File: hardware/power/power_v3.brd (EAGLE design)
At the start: 92 x 92 mm, 32 parts, among them J1 LINEAR_2_5040500291, J2 PWR_2_XT30PW-F, J3 PWR_2_XT30PW-F, J4 PWR_2_XT30PW-F, J5 PWR_2_XT30PW-F, Q1 CSD19536KTT, U1 PDQ30-Q24-S5-D, U2 PDQ30-Q24-S12-D, U3 LM5069

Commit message: Spinning IC
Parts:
- added C12: 0.068uF 50V, _T_rcl:C0603
- added C13: 0.012uF 50V, _T_rcl:C0603
- added D3: SCHOTTKY_SOD123, _T_rcl:SOD123
- added D4: D, _T_rcl:SOD123
- added J10: LINEAR_2_5040500291, _T_conn:MOLEX_5040500291
- added J6, J7: FASTON, _T_power:FASTON_1289-ST
- added J8, J9: PWR_4, _T_conn:MOLEX_4_RA
- added Q2: CSD19536KTT, _T_transistors:TO-263
- added R10: 20k, _T_rcl:R0603
- added R11: 2.4, _T_rcl:R0603
- added R12: 10, _T_rcl:R0603
- added R13: 47k 1%, _T_rcl:R0603
- added R14: 2.7k 1%, _T_rcl:R0603
- added R15: 4.7k 1%, _T_rcl:R0603
- added R16: 1k, _T_rcl:R0603
- added R9: .002, _T_rcl:R2512_KELVIN
- added U4: LM5069, _T_ic:VSSOP_10
- moved C1 92.4 mm to (103.3, 52.3)
- moved C2 92.4 mm to (108.9, 67.8)
- moved D2 92.4 mm to (126.2, 59.9)
- moved R1 92.4 mm to (102.3, 62.1)
- moved R2 92.4 mm to (107.1, 58.6)
- moved R4 92.4 mm to (102.0, 58.6)
- moved R5 92.4 mm to (110.9, 58.6)
- moved R6 92.4 mm to (121.1, 58.6)
- moved R7 92.4 mm to (116.0, 58.6)
- moved U3 92.4 mm to (101.9, 72.3)
- moved D1 92.4 mm to (115.3, 67.3)
- moved R3 92.4 mm to (104.6, 58.6)
- moved R8 92.4 mm to (99.5, 58.6)
- moved L2 37.6 mm to (18.0, 69.0), turned to 90 degrees
- moved C11 34.6 mm to (8.50, 68.5), turned to 180 degrees
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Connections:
- new net N$14: Q2.2, R9.2A, R9.2B
- new net N$15: C12.1, U4.6
- new net N$16: R10.2, U4.7
- new net N$17: R11.1, R12.1, U4.1
- new net N$18: R11.2, R9.2_KELVIN
- new net N$19: R13.1, R14.2, U4.3
- new net N$20: R14.1, R15.2, U4.4
- new net N$21: J10.P1, R13.2
- new net N$22: R12.2, R9.1_KELVIN
- new net N$23: C13.1, D4.C
- new net N$24: D4.A, Q2.1, R16.2, U4.10
- net +12V: now also J9.CIRCUIT2, J9.CIRCUIT4
- net +24V_ISO: now also D3.C, Q2.3, U4.9
- net +5V: now also J8.CIRCUIT2, J8.CIRCUIT4
- net +V_BATT: now also J10.P2, J6.P$1, J6.P$2, R9.1A, R9.1B, U4.2
- net -V_BATT: now also C12.2, C13.2, D3.A, J7.P$1, J7.P$2, R10.1, R15.1, R16.1, U4.5
- net 12V_GND: now also J9.CIRCUIT1, J9.CIRCUIT3
- net 5V_GND: now also J8.CIRCUIT1, J8.CIRCUIT3
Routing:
- net -V_BATT: track 0.00 -> 110.8 mm, vias 0 -> 15
- net N$24: track 0.00 -> 55.9 mm, vias 0 -> 2
- net +12V: track 0.00 -> 43.4 mm
- net +V_BATT: track 0.00 -> 40.9 mm, vias 0 -> 1
- net 12V_GND: track 0.00 -> 39.2 mm
- net N$13: track 0.00 -> 38.7 mm
- net +24V_ISO: track 0.00 -> 36.7 mm
- net N$21: track 0.00 -> 34.5 mm
- net N$22: track 0.00 -> 29.3 mm
- net N$18: track 0.00 -> 26.6 mm
- net 5V_GND: track 0.00 -> 17.7 mm
- net N$17: track 0.00 -> 17.3 mm, vias 0 -> 2
- net N$15: track 0.00 -> 13.1 mm, vias 0 -> 2
- net N$16: track 0.00 -> 11.4 mm, vias 0 -> 2
- net N$19: track 0.00 -> 11.3 mm
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- added copper zone on layer 1, net +24V_ISO
- added copper zone on layer 1, net +24V_POWER
- added copper zone on layer 1, net +V_BATT
- added copper zone on layer 2, net +V_BATT
- added copper zone on layer 1, net N$14

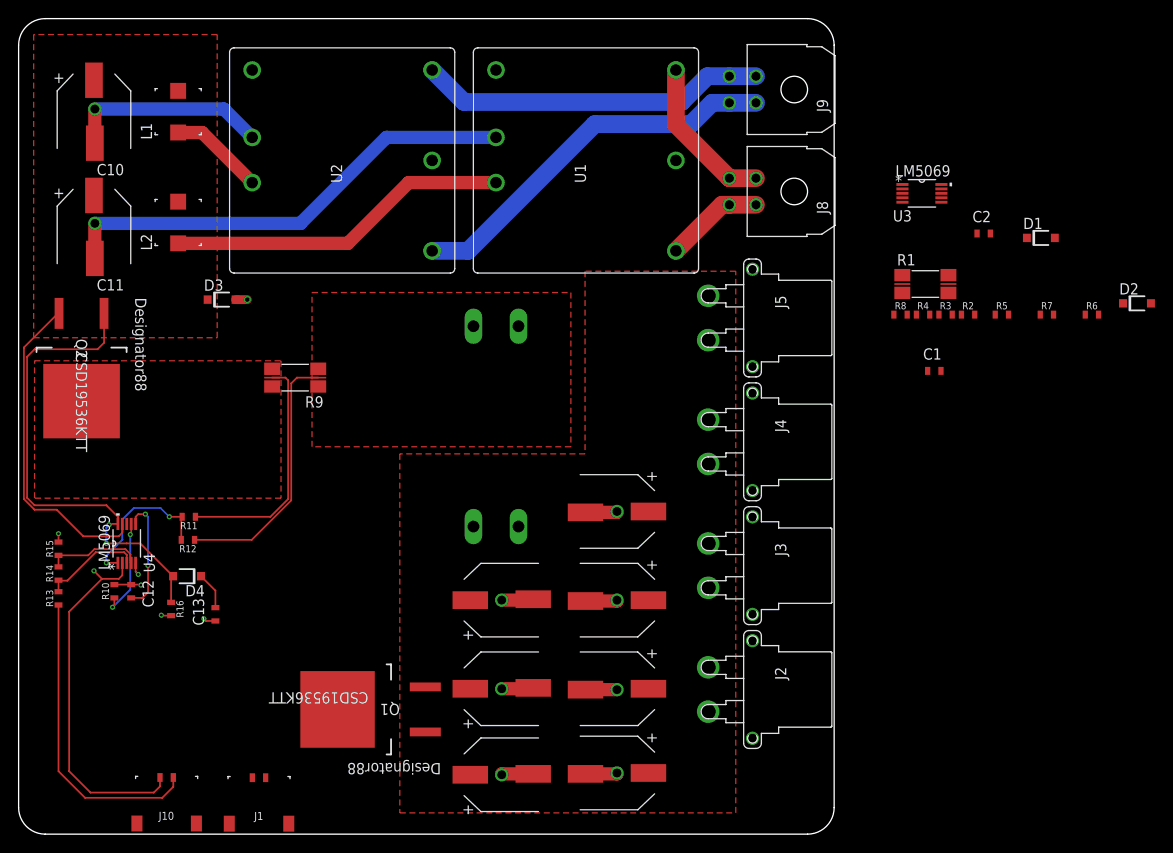
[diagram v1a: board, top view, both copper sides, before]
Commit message: Still need flyback diode
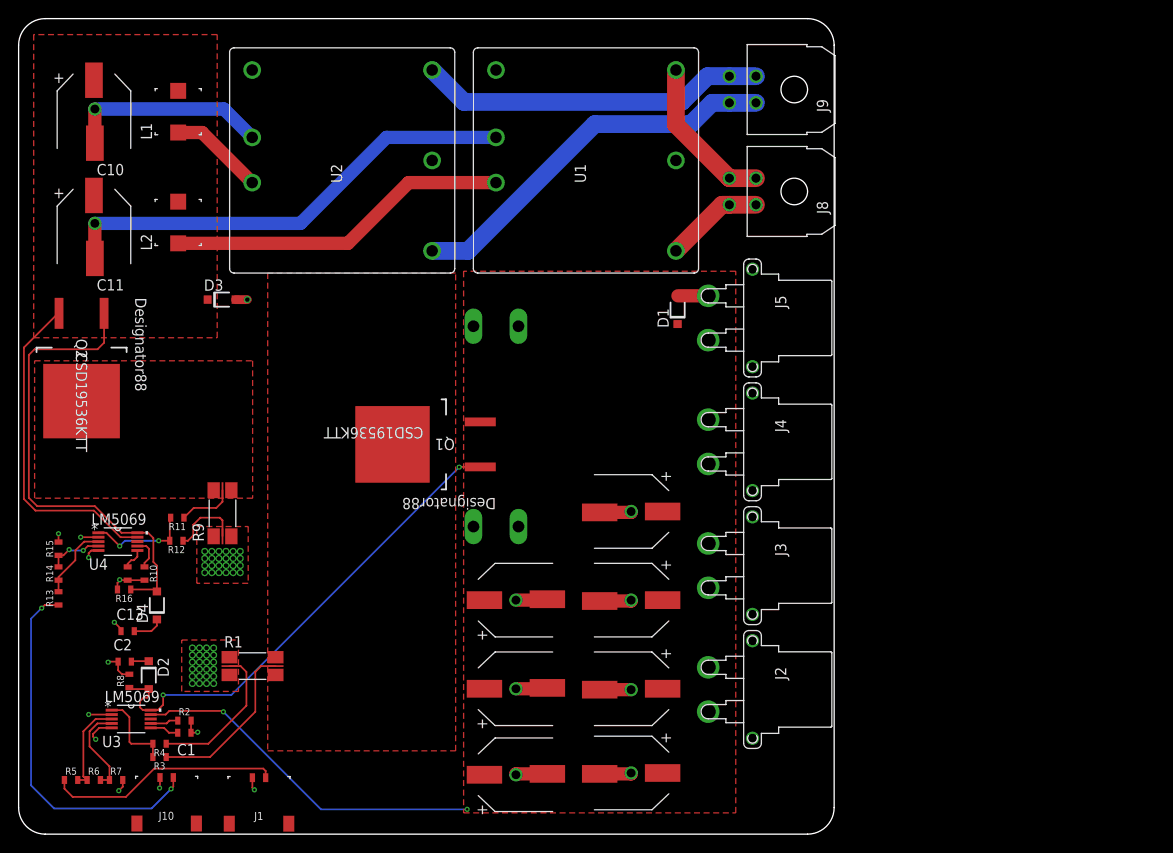
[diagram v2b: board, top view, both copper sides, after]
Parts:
- moved R6 124.2 mm to (8.48, 6.11)
- moved D2 119.1 mm to (14.7, 17.9), turned to 270 degrees
- moved R5 117.4 mm to (5.92, 6.11)
- moved R7 117.4 mm to (11.0, 6.11)
- moved C2 108.3 mm to (12.0, 19.5)
- moved U3 107.1 mm to (12.7, 13.0)
- moved R3 101.8 mm to (15.9, 8.70), turned to 180 degrees
- moved R2 99.6 mm to (18.7, 12.8)
- moved R4 98.8 mm to (15.9, 10.2), turned to 180 degrees
- moved R8 96.3 mm to (12.5, 17.3), turned to 90 degrees
- moved C1 93.9 mm to (18.7, 11.4), turned to 180 degrees
- moved R1 87.3 mm to (26.4, 19.0)
- moved D1 41.8 mm to (74.3, 59.1), turned to 90 degrees
- moved Q1 30.5 mm to (45.9, 44.0)
- moved R9 17.4 mm to (23.0, 36.2), turned to 90 degrees
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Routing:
- net N$2: track 0.00 -> 55.5 mm, vias 0 -> 2
- net +24V_POWER: track 0.00 -> 40.5 mm, vias 0 -> 2
- net +V_BATT: track 40.9 -> 7.29 mm, vias 1 -> 52
- net N$7: track 0.00 -> 26.3 mm
- net N$22: track 29.3 -> 8.15 mm
- net N$18: track 26.6 -> 6.40 mm
- net N$6: track 0.00 -> 19.2 mm
- net N$10: track 0.00 -> 16.8 mm
- net -V_BATT: track 110.8 -> 124.5 mm, vias 15 -> 18
- net N$15: track 13.1 -> 2.48 mm, vias 2 -> 0
- net N$8: track 0.00 -> 10.5 mm
- net N$9: track 0.00 -> 10.3 mm
- net N$5: track 0.00 -> 9.36 mm
- net N$16: track 11.4 -> 3.68 mm, vias 2 -> 0
- net N$21: track 34.5 -> 41.7 mm, vias 0 -> 2
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- added copper zone on layer 1, net N$1

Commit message: TVS diodes
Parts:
- added C14: 0.068uF 50V, _T_rcl:C0603
- added D5: 5_0SMDJ24A, _T_rcl:SOD123
- D1, D3: value SCHOTTKY_SOD123 -> 5_0SMDJ24A
- D2: value D -> (none)
- D4: value D -> 1N4148W-7-F
- moved Q2 5.30 mm to (12.4, 52.7)
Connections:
- net +V_BATT: now also C14.1, D5.C
- net -V_BATT: now also C14.2, D5.A
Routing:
- net N$24: track 53.6 -> 59.0 mm
- net +24V_ISO: track 37.2 -> 42.6 mm
- net +V_BATT: track 7.29 -> 10.6 mm, vias 52 -> 53
- net -V_BATT: track 124.5 -> 127.7 mm, vias 18 -> 19

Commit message: Repositioning rsense
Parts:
- moved R1 6.02 mm to (28.0, 24.8)
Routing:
- net N$10: track 16.8 -> 23.4 mm
- net N$6: track 19.2 -> 25.7 mm

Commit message: Ready to PCB it
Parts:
- D2: value (none) -> 1N4148W-7-F
- moved R3 9.96 mm to (21.1, 17.2)
- moved R4 9.96 mm to (21.1, 18.7)
- moved R1 0.90 mm to (28.0, 23.9)
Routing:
- net N$6: track 25.7 -> 13.5 mm
- net N$10: track 23.4 -> 11.5 mm
- net N$5: track 9.36 -> 12.7 mm, vias 0 -> 2

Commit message: Closer routing iso gate and sense
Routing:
- net N$24: track 59.0 -> 36.8 mm, vias 0 -> 2
- net +24V_ISO: track 42.6 -> 24.6 mm, vias 0 -> 2
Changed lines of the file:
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@@
 </layers>
 <board>
-<fusionsync huburn="a.YnVzaW5lc3M6Z21haWwyMjE5MTc" projecturn="a.YnVzaW5lc3M6Z21haWwyMjE5MTcjMjAxOTA2MjkyMDE0MTU5NzY" f3durn="urn:adsk.wipprod:dm.lineage:NIiH3u5URBCqLPNixwQc4w" pcbguid="" lastpulledtime="2020-07-01T23:36:44Z" lastsyncedchangeguid="" latestrevisionid="139082bc-8da4-45ac-b4e8-9beb6a12b33b" lastsyncedrevisionid="139082bc-8da4-45ac-b4e8-9beb6a12b33b" lastboardhashguid="2a13bf80-225b-326f-a644-5012308f9f45" lastpushedtime="2020-07-03T00:46:42Z" linktopcb3d="true"/>
+<fusionsync huburn="a.YnVzaW5lc3M6Z21haWwyMjE5MTc" projecturn="a.YnVzaW5lc3M6Z21haWwyMjE5MTcjMjAxOTA2MjkyMDE0MTU5NzY" f3durn="urn:adsk.wipprod:dm.lineage:NIiH3u5URBCqLPNixwQc4w" pcbguid="" lastpulledtime="2020-07-01T23:36:44Z" lastsyncedchangeguid="" latestrevisionid="a02dffb8-1203-4a76-a1d6-2f53c010d684" lastsyncedrevisionid="a02dffb8-1203-4a76-a1d6-2f53c010d684" lastboardhashguid="31fae87f-55dd-9496-9b75-db9c020a5965" lastpushedtime="2020-07-03T01:54:28Z" linktopcb3d="true"/>
 <plain>
 <wire x1="3" y1="92" x2="0" y2="89" width="0" layer="20" curve="90" locked="yes"/>
@@
 <vertex x="49.9" y="1.3"/>
 <vertex x="81" y="1.3"/>
-<vertex x="81" y="62.7"/>
-<vertex x="49.9" y="62.7"/>
+<vertex x="81" y="63.2"/>
+<vertex x="49.9" y="63.2"/>
 </polygon>
 </signal>
@@
 <contactref element="Q2" pad="3"/>
 <contactref element="D3" pad="C"/>
-<wire x1="1.9" y1="36.5" x2="0.6" y2="37.8" width="0.2" layer="1"/>
-<wire x1="4.55" y1="58.85" x2="9.86" y2="58.85" width="0.2" layer="1"/>
-<wire x1="0.6" y1="37.8" x2="0.6" y2="54.9" width="0.2" layer="1"/>
-<wire x1="0.6" y1="54.9" x2="4.55" y2="58.85" width="0.2" layer="1"/>
-<wire x1="11.5" y1="33.5" x2="13.3971" y2="33.5" width="0.2" layer="1"/>
-<wire x1="1.9" y1="36.5" x2="8.5" y2="36.5" width="0.2" layer="1"/>
-<wire x1="8.5" y1="36.5" x2="11.5" y2="33.5" width="0.2" layer="1"/>
+<wire x1="13.3971" y1="33.5" x2="12.3" y2="33.5" width="0.2" layer="1"/>
+<wire x1="12.3" y1="33.5" x2="12" y2="33.8" width="0.2" layer="1"/>
+<via x="12" y="33.8" extent="1-16" drill="0.29"/>
+<wire x1="12" y1="33.8" x2="12" y2="56.9" width="0.2" layer="16"/>
+<via x="12" y="56.9" extent="1-16" drill="0.29"/>
 </signal>
 <signal name="12V_GND" class="1">
@@
 <contactref element="Q2" pad="1"/>
 <contactref element="U4" pad="10"/>
-<wire x1="14.94" y1="58.85" x2="14.94" y2="55.44" width="0.2" layer="1"/>
-<wire x1="14.94" y1="55.44" x2="14.2" y2="54.7" width="0.2" layer="1"/>
-<wire x1="1.1524" y1="37.945975" x2="2.0991875" y2="36.9991875" width="0.2" layer="1"/>
-<wire x1="8.6008125" y1="36.9991875" x2="2.0991875" y2="36.9991875" width="0.2" layer="1"/>
-<wire x1="14.2" y1="54.7" x2="1.8" y2="54.7" width="0.2" layer="1"/>
-<wire x1="1.8" y1="54.7" x2="1.1524" y2="54.0524" width="0.2" layer="1"/>
-<wire x1="1.1524" y1="54.0524" x2="1.1524" y2="37.945975" width="0.2" layer="1"/>
 <wire x1="12.65" y1="27.6" x2="15.375" y2="27.6" width="0.2" layer="1"/>
 <wire x1="15.375" y1="27.6" x2="15.6" y2="27.375" width="0.2" layer="1"/>
-<wire x1="13.3971" y1="34" x2="11.6" y2="34" width="0.2" layer="1"/>
-<wire x1="11.6" y1="34" x2="8.6008125" y2="36.9991875" width="0.2" layer="1"/>
 <wire x1="15.6" y1="27.375" x2="15.6" y2="30.3" width="0.2" layer="1"/>
 <wire x1="15.2" y1="30.7" x2="15.2" y2="33.4" width="0.2" layer="1"/>
@@
 <wire x1="14.6" y1="34" x2="13.3971" y2="34" width="0.2" layer="1"/>
 <wire x1="15.6" y1="30.3" x2="15.2" y2="30.7" width="0.2" layer="1"/>
+<wire x1="13.3971" y1="34" x2="13.3971" y2="36.6971" width="0.2" layer="1"/>
+<wire x1="13.3971" y1="36.6971" x2="13.4" y2="36.7" width="0.2" layer="1"/>
+<via x="13.4" y="36.7" extent="1-16" drill="0.29"/>
+<wire x1="13.4" y1="36.7" x2="13.4" y2="53.4" width="0.2" layer="16"/>
+<wire x1="13.4" y1="53.4" x2="14.9" y2="54.9" width="0.2" layer="16"/>
+<via x="14.9" y="54.9" extent="1-16" drill="0.29"/>
+<wire x1="14.9" y1="54.9" x2="14.9" y2="58.81" width="0.2" layer="1"/>
+<wire x1="14.9" y1="58.81" x2="14.94" y2="58.85" width="0.2" layer="1"/>
 </signal>
 </signals>

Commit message: Power junctions
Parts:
- moved J8 0.30 mm to (87.2, 72.5)
- moved J9 0.30 mm to (87.2, 84.0)
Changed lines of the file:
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@@
 <attribute name="NAME" x="57.66" y="37.24" locked="yes" size="1.27" layer="22" rot="MR0"/>
 </element>
-<element name="J8" library="_T_conn" library_urn="urn:adsk.eagle:library:19570503" package="MOLEX_4_RA" package3d_urn="urn:adsk.eagle:package:16152611/5" value="PWR_4" x="87.5" y="72.5" smashed="yes" rot="R90">
-<attribute name="NAME" x="91.31" y="69.96" size="1.27" layer="25" rot="R90"/>
-</element>
-<element name="J9" library="_T_conn" library_urn="urn:adsk.eagle:library:19570503" package="MOLEX_4_RA" package3d_urn="urn:adsk.eagle:package:16152611/5" value="PWR_4" x="87.5" y="84" smashed="yes" rot="R90">
-<attribute name="NAME" x="91.31" y="81.46" size="1.27" layer="25" rot="R90"/>
+<element name="J8" library="_T_conn" library_urn="urn:adsk.eagle:library:19570503" package="MOLEX_4_RA" package3d_urn="urn:adsk.eagle:package:16152611/5" value="PWR_4" x="87.2" y="72.5" smashed="yes" rot="R90">
+<attribute name="NAME" x="91.01" y="69.96" size="1.27" layer="25" rot="R90"/>
+</element>
+<element name="J9" library="_T_conn" library_urn="urn:adsk.eagle:library:19570503" package="MOLEX_4_RA" package3d_urn="urn:adsk.eagle:package:16152611/5" value="PWR_4" x="87.2" y="84" smashed="yes" rot="R90">
+<attribute name="NAME" x="91.01" y="81.46" size="1.27" layer="25" rot="R90"/>
 </element>
 <element name="U4" library="_T_ic" library_urn="urn:adsk.eagle:library:19571245" package="VSSOP_10" package3d_urn="urn:adsk.eagle:package:21297470/2" value="LM5069" x="11.2" y="33" smashed="yes">
@@
 <contactref element="J9" pad="CIRCUIT3"/>
 <wire x1="46.65" y1="86.2" x2="50.25" y2="82.6" width="2" layer="16"/>
-<wire x1="77.7" y1="85.5" x2="80.18" y2="85.5" width="2" layer="16"/>
+<wire x1="77.7" y1="85.5" x2="79.88" y2="85.5" width="2" layer="16"/>
 <wire x1="50.25" y1="82.6" x2="74.8" y2="82.6" width="2" layer="16"/>
 <wire x1="74.8" y1="82.6" x2="77.7" y2="85.5" width="2" layer="16"/>
-<wire x1="83.18" y1="85.5" x2="80.18" y2="85.5" width="2" layer="16"/>
+<wire x1="82.88" y1="85.5" x2="79.88" y2="85.5" width="2" layer="16"/>
 </signal>
 <signal name="5V_GND" class="1">
@@
 <contactref element="J8" pad="CIRCUIT3"/>
 <contactref element="J8" pad="CIRCUIT1"/>
-<wire x1="83.18" y1="74" x2="80.18" y2="74" width="2" layer="1"/>
-<wire x1="80.18" y1="74" x2="74.15" y2="80.03" width="2" layer="1"/>
-<wire x1="74.15" y1="80.03" x2="74.15" y2="86.2" width="2" layer="1"/>
+<wire x1="82.88" y1="74" x2="79.88" y2="74" width="2" layer="1"/>
+<wire x1="79.88" y1="74" x2="74.15" y2="79.73" width="2" layer="1"/>
+<wire x1="74.15" y1="79.73" x2="74.15" y2="86.2" width="2" layer="1"/>
 </signal>
 <signal name="+12V" class="1">
@@
 <contactref element="J9" pad="CIRCUIT4"/>
 <contactref element="J9" pad="CIRCUIT2"/>
-<wire x1="83.182" y1="82.5" x2="80.18" y2="82.5" width="2" layer="16"/>
-<wire x1="80.18" y1="82.5" x2="78.2355375" y2="82.5" width="2" layer="16"/>
+<wire x1="82.882" y1="82.5" x2="79.88" y2="82.5" width="2" layer="16"/>
+<wire x1="79.88" y1="82.5" x2="78.2355375" y2="82.5" width="2" layer="16"/>
 <wire x1="78.2355375" y1="82.5" x2="75.8355375" y2="80.1" width="2" layer="16"/>
 <wire x1="75.8355375" y1="80.1" x2="65" y2="80.1" width="2" layer="16"/>
@@
 <contactref element="J8" pad="CIRCUIT2"/>
 <wire x1="74.15" y1="65.8" x2="79.35" y2="71" width="2" layer="1"/>
-<wire x1="79.35" y1="71" x2="80.18" y2="71" width="2" layer="1"/>
-<wire x1="80.18" y1="71" x2="83.182" y2="71" width="2" layer="1"/>
+<wire x1="79.35" y1="71" x2="79.88" y2="71" width="2" layer="1"/>
+<wire x1="79.88" y1="71" x2="82.882" y2="71" width="2" layer="1"/>
 </signal>
 <signal name="N$14">

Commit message: Mounting holes
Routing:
- net -V_BATT: vias 19 -> 22
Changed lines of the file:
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@@
 </layers>
 <board>
-<fusionsync huburn="a.YnVzaW5lc3M6Z21haWwyMjE5MTc" projecturn="a.YnVzaW5lc3M6Z21haWwyMjE5MTcjMjAxOTA2MjkyMDE0MTU5NzY" f3durn="urn:adsk.wipprod:dm.lineage:NIiH3u5URBCqLPNixwQc4w" pcbguid="" lastpulledtime="2020-07-01T23:36:44Z" lastsyncedchangeguid="" latestrevisionid="a02dffb8-1203-4a76-a1d6-2f53c010d684" lastsyncedrevisionid="a02dffb8-1203-4a76-a1d6-2f53c010d684" lastboardhashguid="31fae87f-55dd-9496-9b75-db9c020a5965" lastpushedtime="2020-07-03T01:54:28Z" linktopcb3d="true"/>
+<fusionsync huburn="a.YnVzaW5lc3M6Z21haWwyMjE5MTc" projecturn="a.YnVzaW5lc3M6Z21haWwyMjE5MTcjMjAxOTA2MjkyMDE0MTU5NzY" f3durn="urn:adsk.wipprod:dm.lineage:NIiH3u5URBCqLPNixwQc4w" pcbguid="" lastpulledtime="2020-07-01T23:36:44Z" lastsyncedchangeguid="" latestrevisionid="530ae671-e04d-4b38-93bb-567a0a173544" lastsyncedrevisionid="530ae671-e04d-4b38-93bb-567a0a173544" lastboardhashguid="b9e23031-b94e-cb52-fadd-b5d31641fdc8" lastpushedtime="2020-07-03T02:13:44Z" linktopcb3d="true"/>
 <plain>
 <wire x1="3" y1="92" x2="0" y2="89" width="0" layer="20" curve="90" locked="yes"/>
@@
 <wire x1="92" y1="89" x2="89" y2="92" width="0" layer="20" curve="90" locked="yes"/>
 <wire x1="3" y1="92" x2="89" y2="92" width="0" layer="20" locked="yes"/>
+<circle x="89" y="89" radius="3" width="0.2" layer="21"/>
+<circle x="46" y="89" radius="3" width="0.2" layer="21"/>
+<circle x="3" y="89" radius="3" width="0.2" layer="21"/>
+<circle x="89" y="3" radius="3" width="0.2" layer="21"/>
+<circle x="46" y="3" radius="3" width="0.2" layer="21"/>
+<circle x="3" y="3" radius="3" width="0.2" layer="21"/>
 </plain>
 <attributes>
@@
 <wire x1="44.2" y1="4.525" x2="44.175" y2="4.5" width="0.2" layer="1"/>
 <wire x1="44.175" y1="4.5" x2="41.9" y2="4.5" width="1" layer="1"/>
+<via x="89" y="89" extent="1-16" drill="3"/>
+<via x="3" y="89" extent="1-16" drill="3"/>
+<via x="46" y="89" extent="1-16" drill="3"/>
 </signal>
 <signal name="N$10">
@@
 <wire x1="14.9" y1="58.81" x2="14.94" y2="58.85" width="0.2" layer="1"/>
 </signal>
+<signal name="-V_BATT1">
+<via x="89" y="3" extent="1-16" drill="3"/>
+<via x="3" y="3" extent="1-16" drill="3"/>
+<via x="46" y="3" extent="1-16" drill="3"/>
+<wire x1="46" y1="3" x2="89" y2="3" width="0" layer="19" extent="1-1"/>
+<wire x1="3" y1="3" x2="46" y2="3" width="0" layer="19" extent="1-1"/>
+</signal>
 </signals>
